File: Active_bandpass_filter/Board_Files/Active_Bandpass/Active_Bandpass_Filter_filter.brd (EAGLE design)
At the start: 100 x 80 mm, 18 parts, among them IC1 AD8542R, IC2 AD8031R, IC3 7805TV

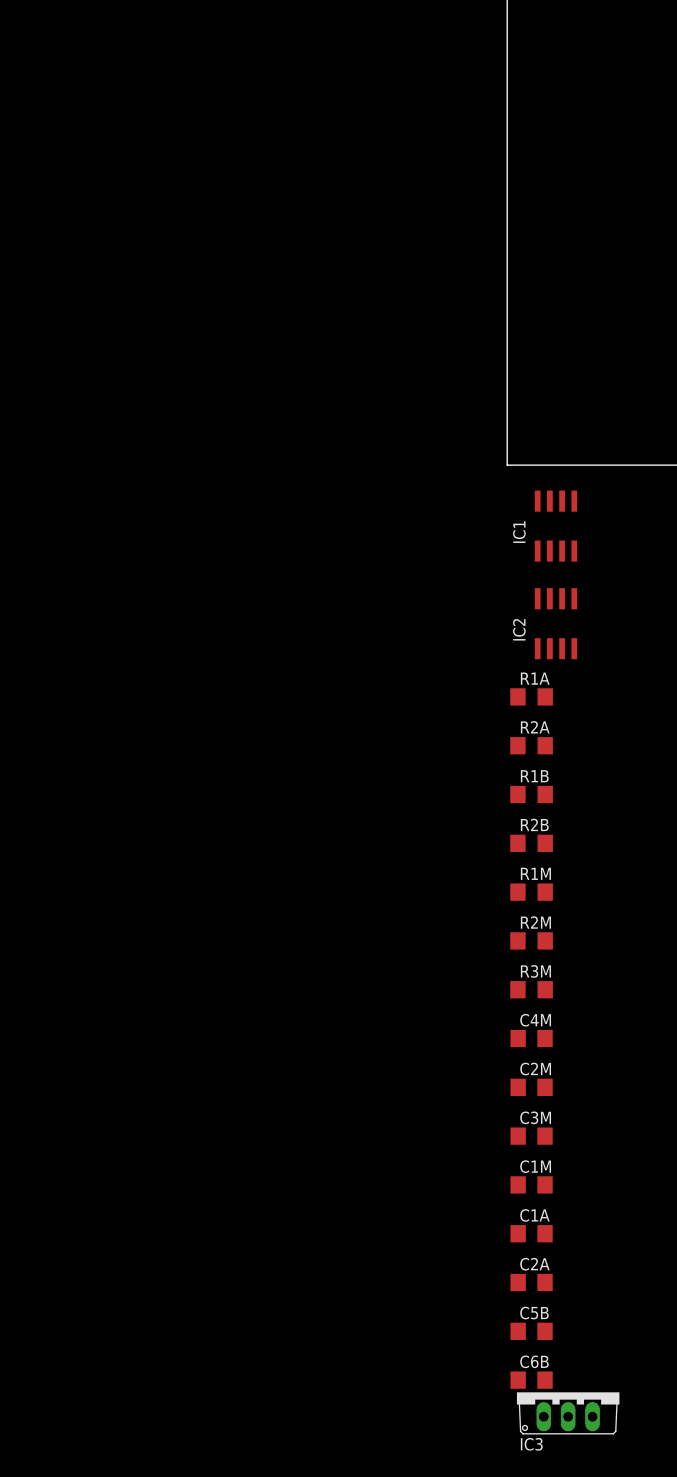
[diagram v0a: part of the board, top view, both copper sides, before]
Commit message: split into 2 boards
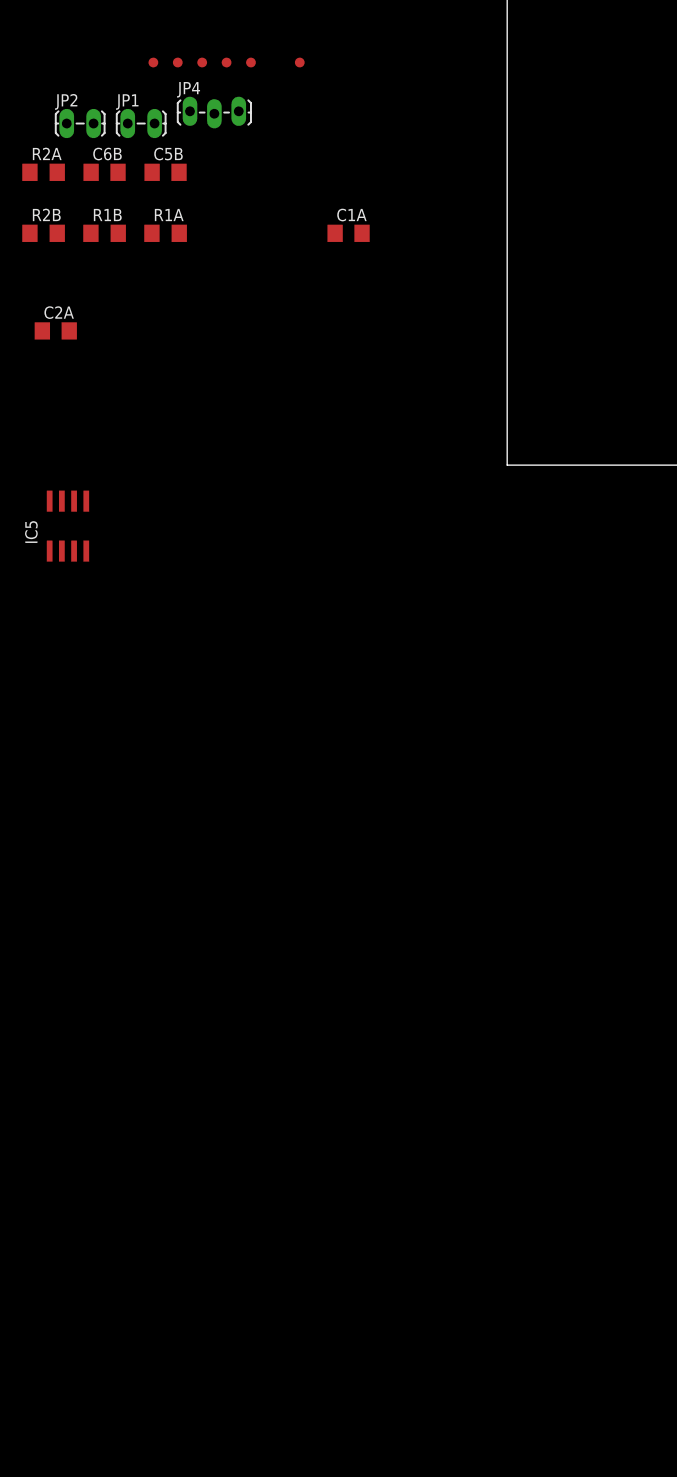
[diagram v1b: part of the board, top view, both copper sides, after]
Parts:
- removed C1M, C2M, C3M, C4M: (no value), resistor:C1206
- removed IC1: AD8542R, analog-devices:SO8
- removed IC2: AD8031R, analog-devices:SO8
- removed IC3: 7805TV, linear:TO220V
- removed R1M, R2M: (no value), resistor:R1206
- removed R3M: (no value), rcl:R1206
- added IC5: AD8542R, analog-devices:SO8
- added JP1, JP2: (no value), SparkFun-Connectors:1X02_LOCK_LONGPADS
- added JP4: (no value), SparkFun-Connectors:1X03_LOCK_LONGPADS
- added TP1, TP3, TP4, TP5, TP6, TP7: TEST-POINT3X4, SparkFun-Passives:PAD.03X.04
- C1A: value (none) -> 3.9nF
- C2A: value (none) -> 390pF
- C5B, C6B: value (none) -> 68nF
- R1A: value (none) -> 8.45k
- R1B: value (none) -> 6.34k
- R2A: value (none) -> 118k
- R2B: value (none) -> 15.8k
- moved C6B 133.4 mm to (-41.9, 30.5)
- moved C5B 126.5 mm to (-35.6, 30.5)
- moved C2A 110.8 mm to (-47.0, 14.0)
- moved C1A 105.9 mm to (-16.5, 24.1)
- moved R2B 81.3 mm to (-48.3, 24.1)
- moved R2A 78.4 mm to (-48.3, 30.5)
- moved R1B 73.4 mm to (-41.9, 24.1)
- moved R1A 61.5 mm to (-35.6, 24.1)
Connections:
- removed net N$12: IC2.2, R3M.1
- removed net N$6: IC1.6, IC1.7, R1B.2
- removed net N$8: C1M.1, C4M.1, IC2.3, R1M.1, R2M.2
- removed net V+: IC1.8
- removed net V-: IC1.4
- removed net VCC: IC3.1
- new net SIG-IN: JP1.2
- new net SIG_IN: R1A.1, TP3.P$1
- new net SIG_OUT: IC5.6, IC5.7, JP2.2, R1B.2, TP5.P$1
- net 5V: now also IC5.8, JP4.1, TP6.P$1; no longer IC2.7, IC3.3, R1M.2
- net GND: now also IC5.4, JP1.1, JP2.1, JP4.2, TP7.P$1; no longer C1M.2, C2M.2, C3M.2, C4M.2, IC2.4, IC3.2, R2M.1
- net N$2: now also IC5.3; no longer IC1.3
- net N$3: now also IC5.1, IC5.2, TP1.P$1; no longer IC1.1, IC1.2
- net N$5: now also IC5.5; no longer IC1.5
- net REF: now also JP4.3, TP4.P$1; no longer C2M.1, C3M.1, IC2.6, R1A.1, R3M.2

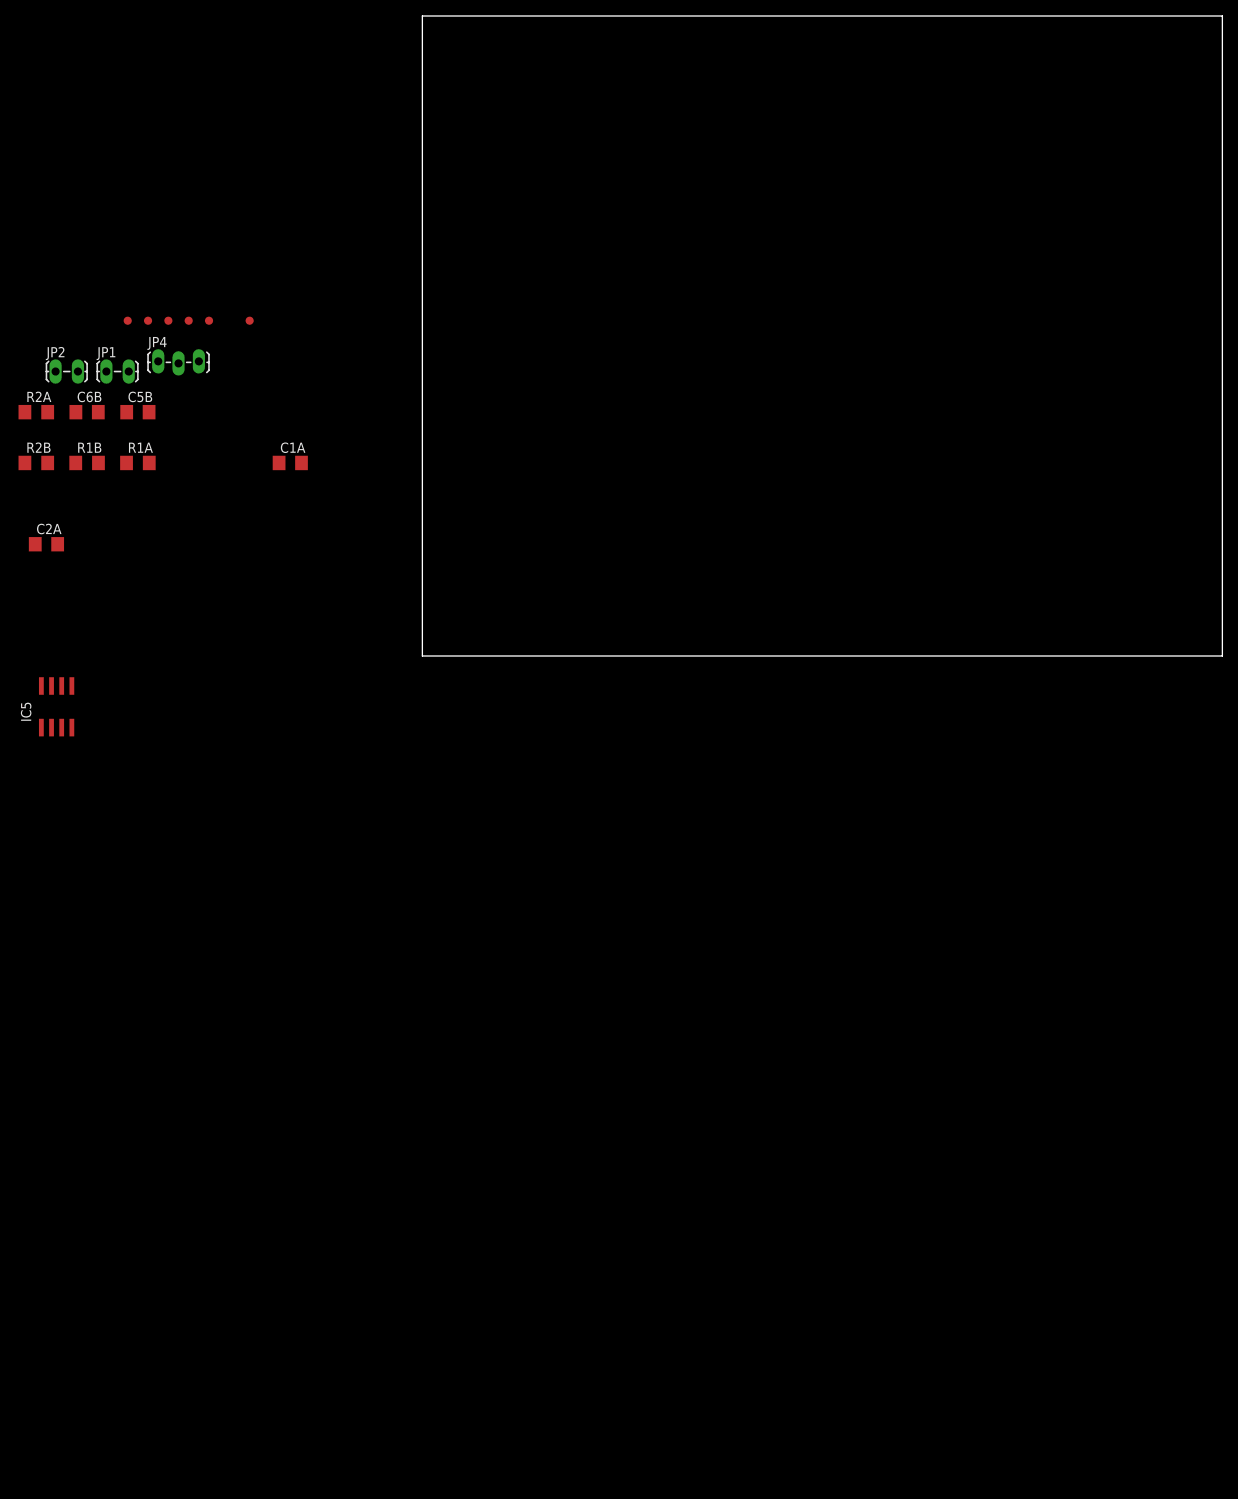
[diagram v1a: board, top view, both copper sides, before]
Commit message: Initial board buildup for individual filter board
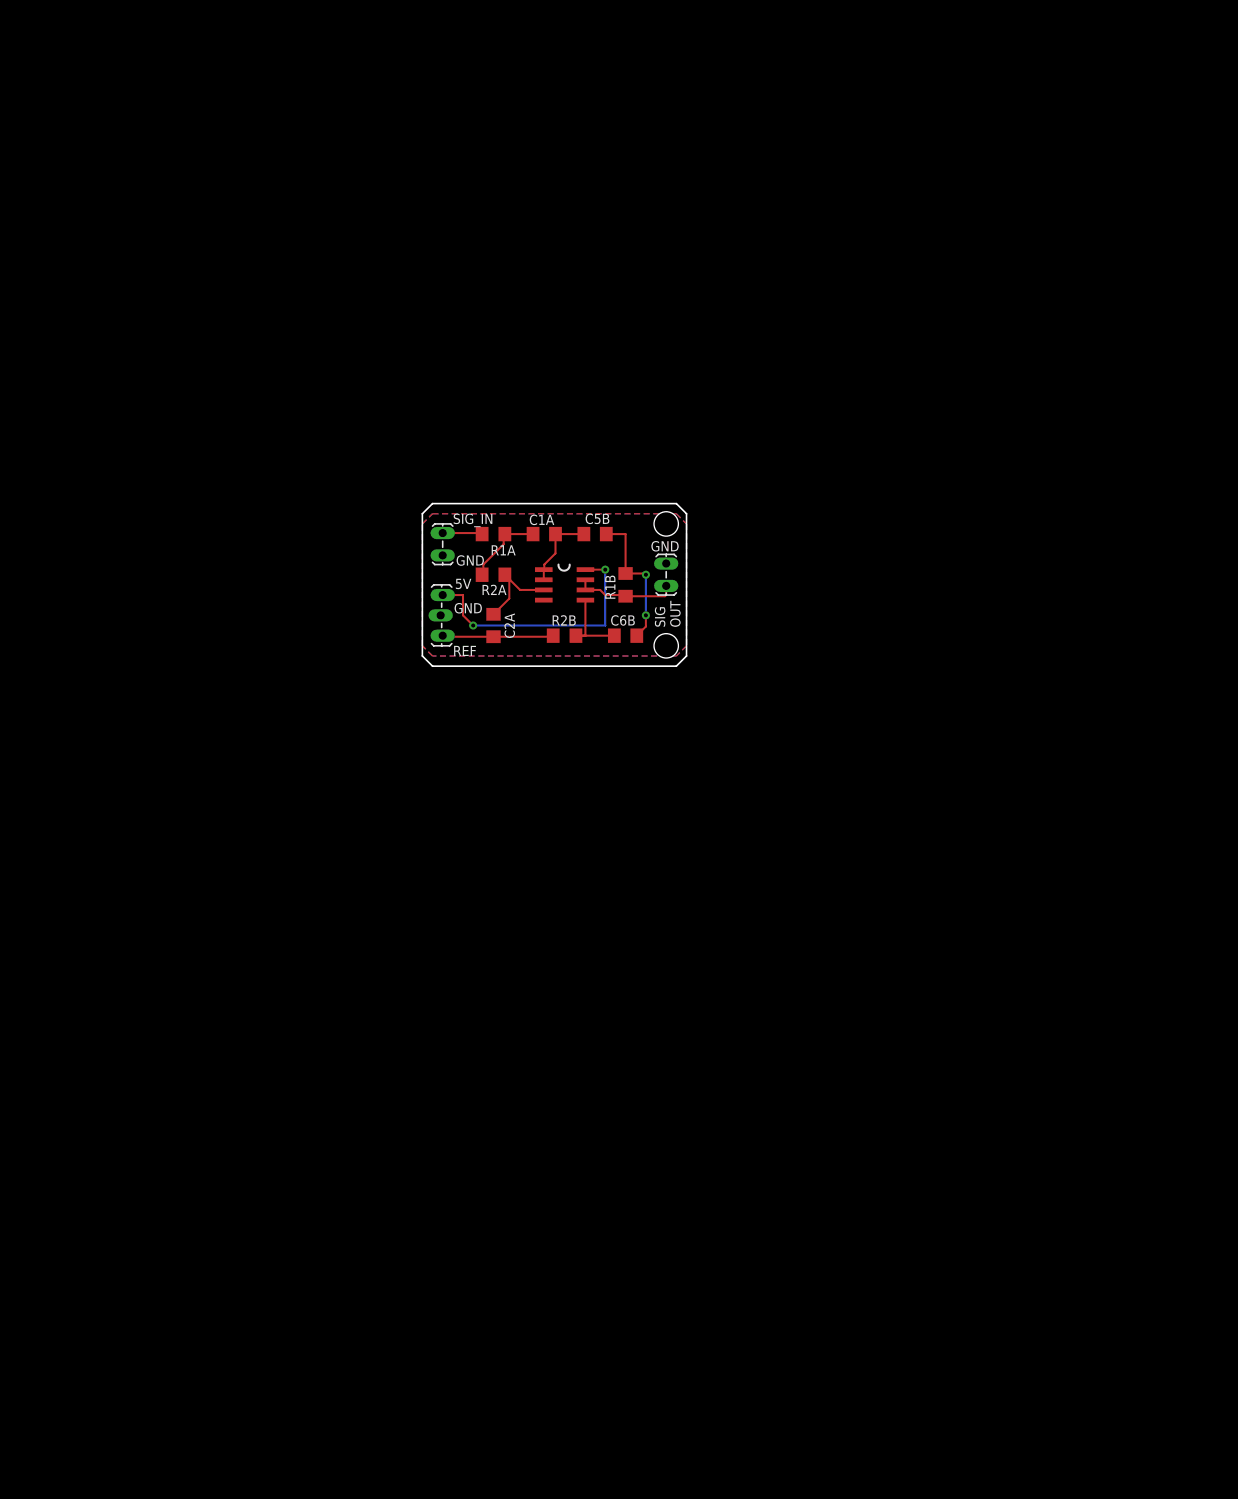
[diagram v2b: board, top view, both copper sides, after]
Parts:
- removed TP1, TP3, TP4, TP5, TP6, TP7: TEST-POINT3X4, SparkFun-Passives:PAD.03X.04
- moved JP2 79.9 mm to (30.5, 11.4), turned to 270 degrees
- moved C6B 72.9 mm to (25.4, 2.54), turned to 180 degrees
- moved R2B 69.5 mm to (17.8, 2.54)
- moved R1B 69.0 mm to (25.4, 8.89), turned to 270 degrees
- moved IC5 65.3 mm to (17.8, 8.89), turned to 270 degrees
- moved R2A 60.7 mm to (8.89, 10.2)
- moved C5B 59.1 mm to (21.6, 15.2)
- moved C2A 56.8 mm to (8.89, 3.81), turned to 270 degrees
- moved JP1 47.7 mm to (2.54, 12.7), turned to 90 degrees
- moved JP4 46.0 mm to (2.54, 7.62), turned to 270 degrees
- moved R1A 45.3 mm to (8.89, 15.2)
- moved C1A 33.0 mm to (15.2, 15.2)
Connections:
- removed net SIG-IN: JP1.2
- net 5V: no longer TP6.P$1
- net GND: no longer TP7.P$1
- net N$3: no longer TP1.P$1
- net REF: no longer TP4.P$1
- net SIG_IN: now also JP1.2; no longer TP3.P$1
- net SIG_OUT: no longer TP5.P$1
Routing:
- net 5V: track 0.00 -> 32.9 mm, vias 0 -> 2
- net N$4: track 0.00 -> 18.1 mm, vias 0 -> 2
- net REF: track 0.00 -> 13.9 mm
- net SIG_OUT: track 0.00 -> 12.9 mm
- net N$2: track 0.00 -> 10.9 mm
- net N$5: track 0.00 -> 10.4 mm
- net N$1: track 0.00 -> 9.88 mm
- net N$3: track 0.00 -> 9.87 mm
- net SIG_IN: track 0.00 -> 5.06 mm
- added copper zone on layer 1, net GND
- added copper zone on layer 16, net GND
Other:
- board size 100 x 80 mm -> 33 x 20.3 mm
- board text added: "5V"
- board text added: "Bandpass Filter v1.0 12-2015 M Stebbins"
- board text added: "GND"
- board text added: "REF"
- board text added: "SIG OUT"
- board text added: "SIG_IN"
